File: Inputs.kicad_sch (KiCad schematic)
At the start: 2 parts, among them J14 Digital Inputs

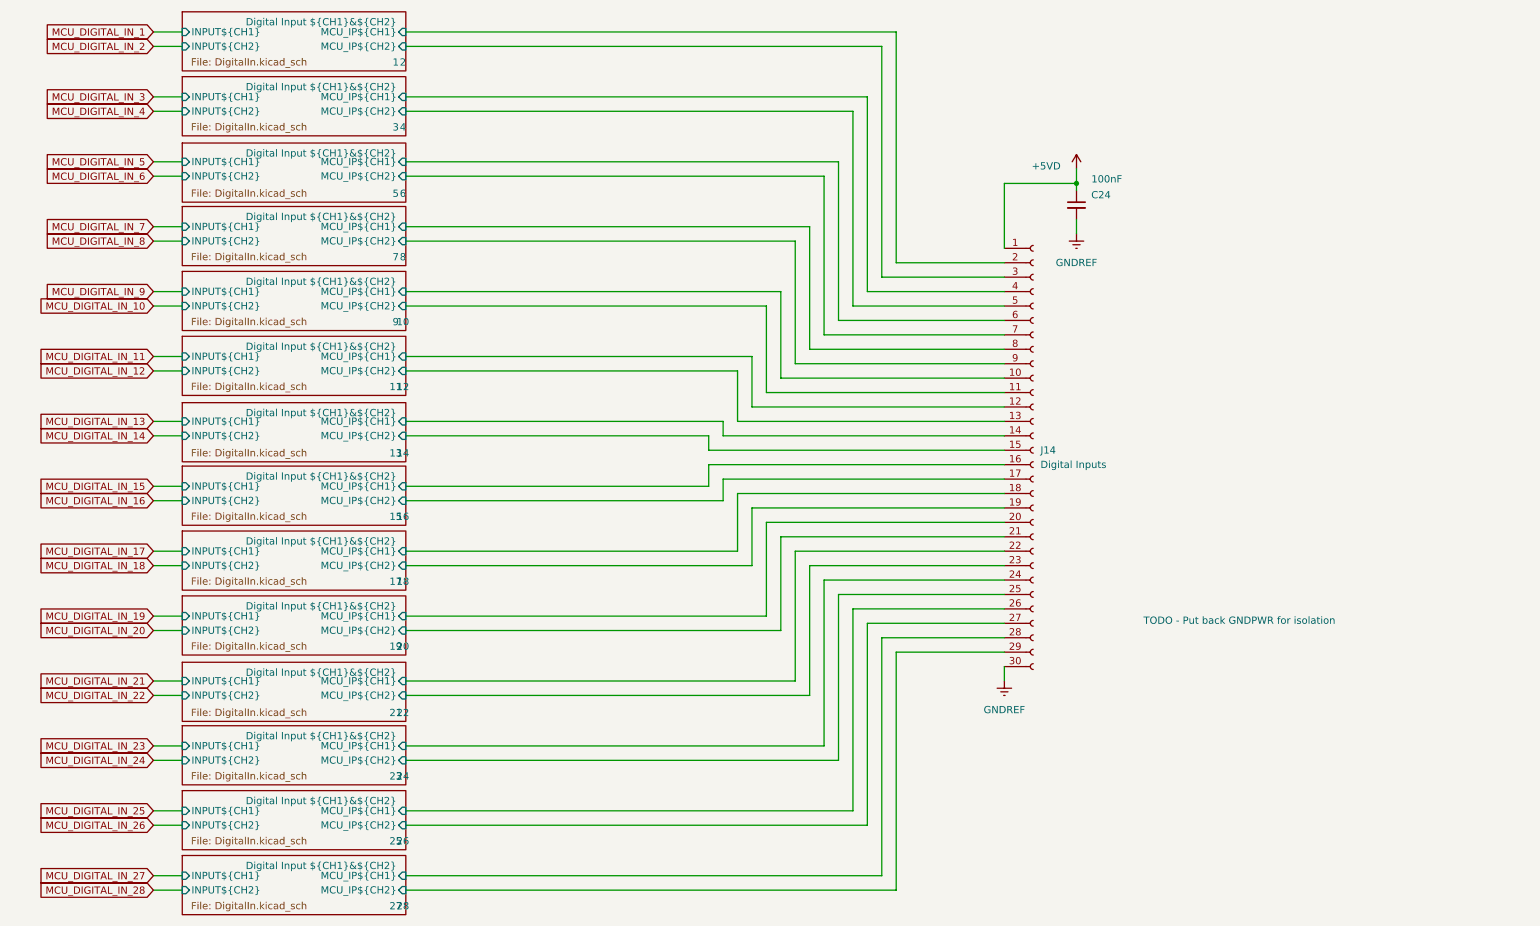
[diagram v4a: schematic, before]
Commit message: Dropped number of IO on design to make more room. Created the new footprints to suit them, updates to BOM and ran some traces on the PCB.
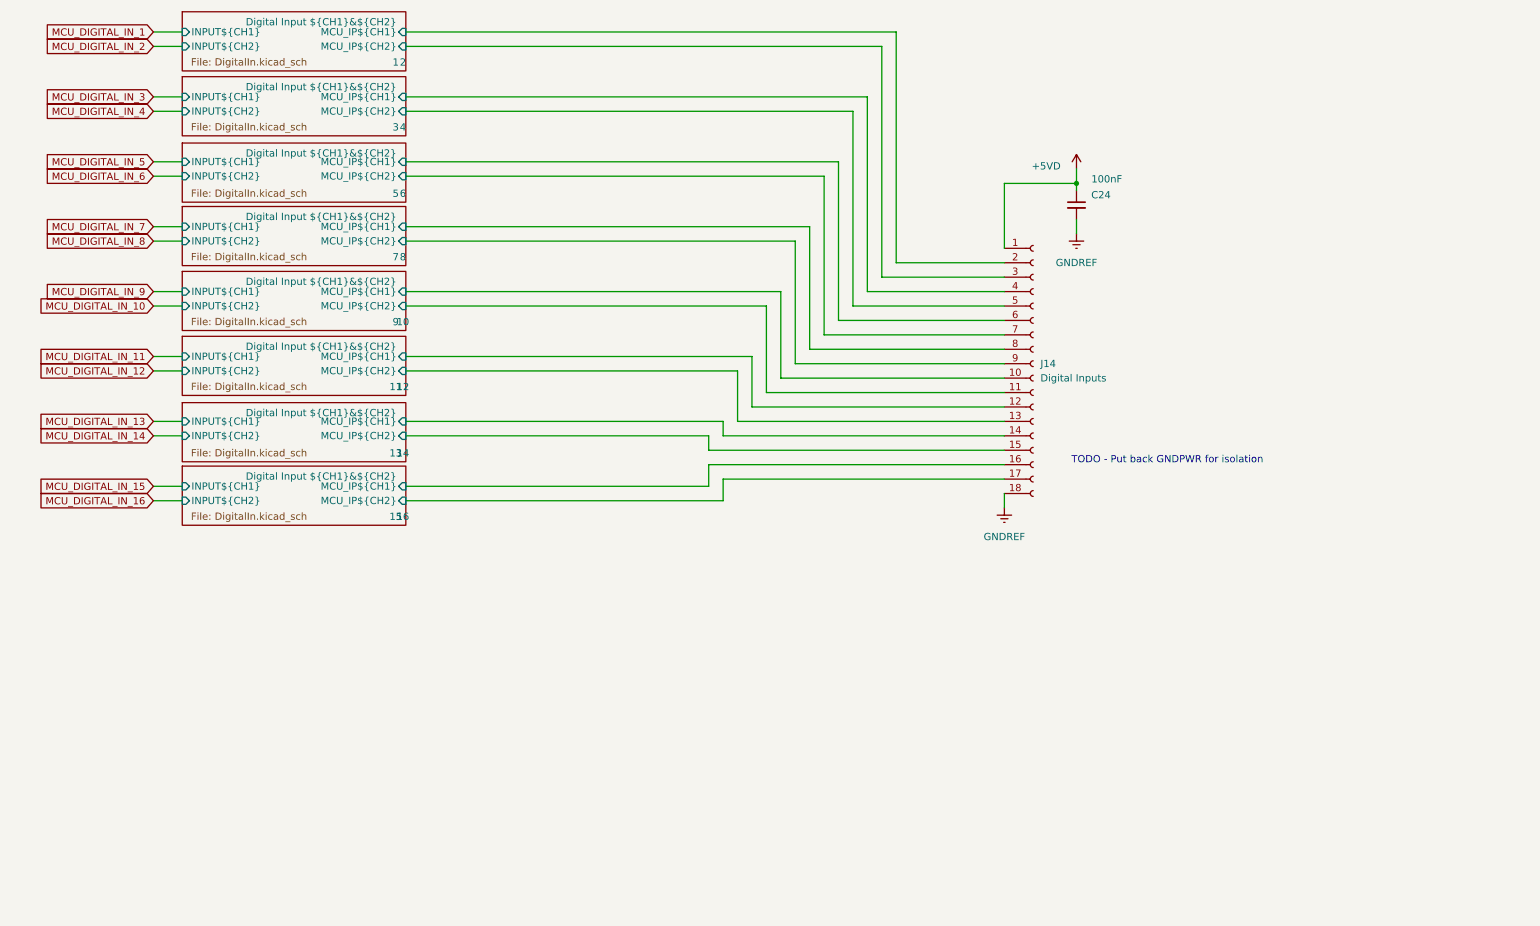
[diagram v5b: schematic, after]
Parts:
- J14: footprint EBWA_06_A:CONN_EBWA-30-A_ADM -> EBWA_06_A:CONN_EBWA-18-A_ADM; symbol Connector:Conn_01x30_Socket -> Connector:Conn_01x18_Socket
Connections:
- net Digital Input ${CH1}&${CH2}/MCU_IP${CH1} is gone; now on net GNDREF: J14.18 (Pin_18)
- net Digital Input ${CH1}&${CH2}/MCU_IP${CH1} is gone; now on net Digital Input ${CH1}&${CH2}/MCU_IP${CH1}: J14.8 (Pin_8)
- net Digital Input ${CH1}&${CH2}/MCU_IP${CH2} is gone; now on net Digital Input ${CH1}&${CH2}/MCU_IP${CH2}: J14.9 (Pin_9)
- net Digital Input ${CH1}&${CH2}/MCU_IP${CH1}: no longer J14.10 (Pin_10)
- net Digital Input ${CH1}&${CH2}/MCU_IP${CH2}: no longer J14.11 (Pin_11)
- net GNDREF: no longer J14.30 (Pin_30)
- removed net Digital Input ${CH1}&${CH2}/MCU_IP${CH1}: J14.20 (Pin_20)
- removed net Digital Input ${CH1}&${CH2}/MCU_IP${CH1}: J14.22 (Pin_22)
- removed net Digital Input ${CH1}&${CH2}/MCU_IP${CH1}: J14.24 (Pin_24)
- removed net Digital Input ${CH1}&${CH2}/MCU_IP${CH1}: J14.26 (Pin_26)
- removed net Digital Input ${CH1}&${CH2}/MCU_IP${CH1}: J14.28 (Pin_28)
- removed net Digital Input ${CH1}&${CH2}/MCU_IP${CH2}: J14.19 (Pin_19)
- removed net Digital Input ${CH1}&${CH2}/MCU_IP${CH2}: J14.21 (Pin_21)
- removed net Digital Input ${CH1}&${CH2}/MCU_IP${CH2}: J14.23 (Pin_23)
- removed net Digital Input ${CH1}&${CH2}/MCU_IP${CH2}: J14.25 (Pin_25)
- removed net Digital Input ${CH1}&${CH2}/MCU_IP${CH2}: J14.27 (Pin_27)
- removed net Digital Input ${CH1}&${CH2}/MCU_IP${CH2}: J14.29 (Pin_29)
- new net Digital Input ${CH1}&${CH2}/MCU_IP${CH1}: J14.10 (Pin_10)
- new net Digital Input ${CH1}&${CH2}/MCU_IP${CH2}: J14.11 (Pin_11)

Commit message: New optocoupler part choice, removed digikey BOM as have started inputting them into symbol fields. Re-enabled all disabled parts for now and will re-design power supplies soon.
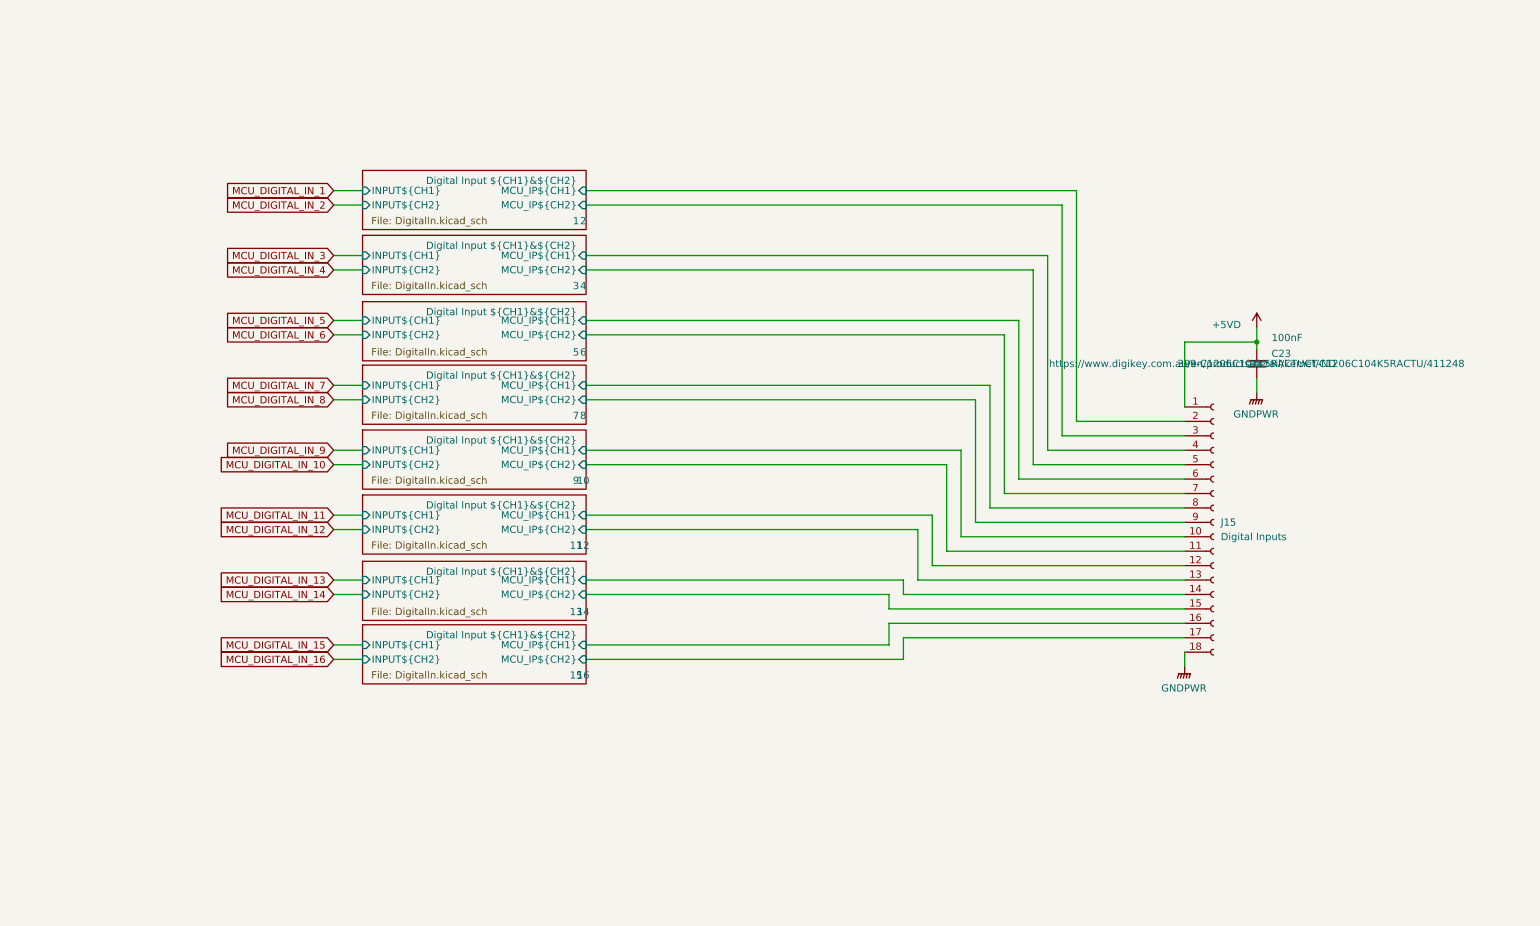
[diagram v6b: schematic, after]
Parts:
- C23: renamed from C24; Digikey Part Number (none) -> 399-C1206C104K5RACTUCT-ND; Digikey URL (none) -> https://www.digikey.com.au/en/products/detail/kemet/C1206C1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
- renumbered J14 to J15
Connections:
- net Digital Input ${CH1}&${CH2}/MCU_IP${CH1} is gone; now on net Digital Input ${CH1}&${CH2}/MCU_IP${CH1}: J15.8 (Pin_8)
- net Digital Input ${CH1}&${CH2}/MCU_IP${CH2} is gone; now on net Digital Input ${CH1}&${CH2}/MCU_IP${CH2}: J15.9 (Pin_9)
- net Digital Input ${CH1}&${CH2}/MCU_IP${CH1}: no longer J15.10 (Pin_10)
- net Digital Input ${CH1}&${CH2}/MCU_IP${CH2}: no longer J15.11 (Pin_11)
- net GNDREF renamed GNDPWR
- new net Digital Input ${CH1}&${CH2}/MCU_IP${CH1}: J15.10 (Pin_10)
- new net Digital Input ${CH1}&${CH2}/MCU_IP${CH2}: J15.11 (Pin_11)
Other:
- note removed: "TODO - Put back GNDPWR for isolation"
- moved on the sheet: C23, J15

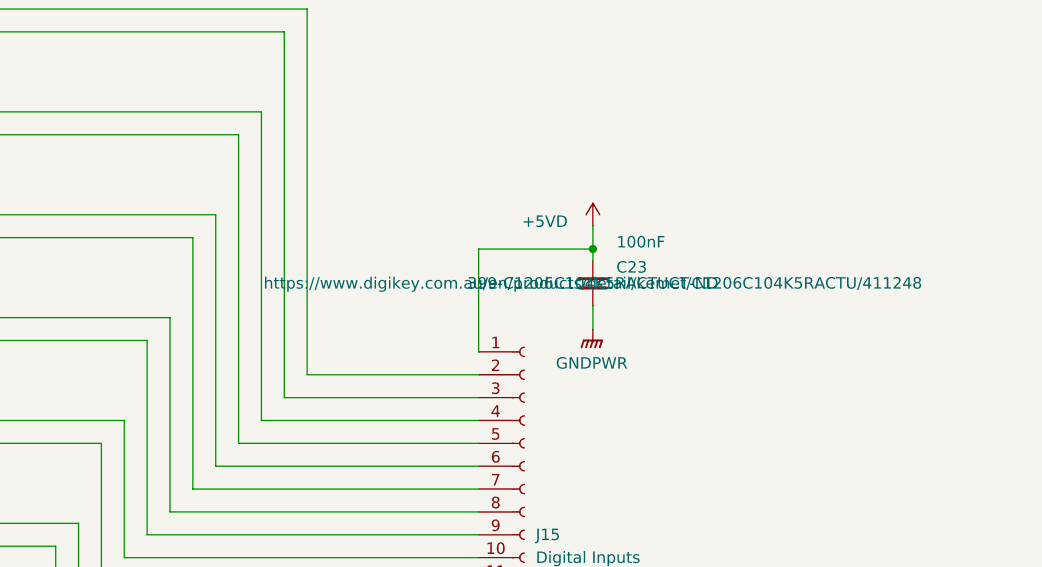
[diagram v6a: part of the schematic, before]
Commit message: fix to annoying additional symbol fields displaying when we didn't want them to.
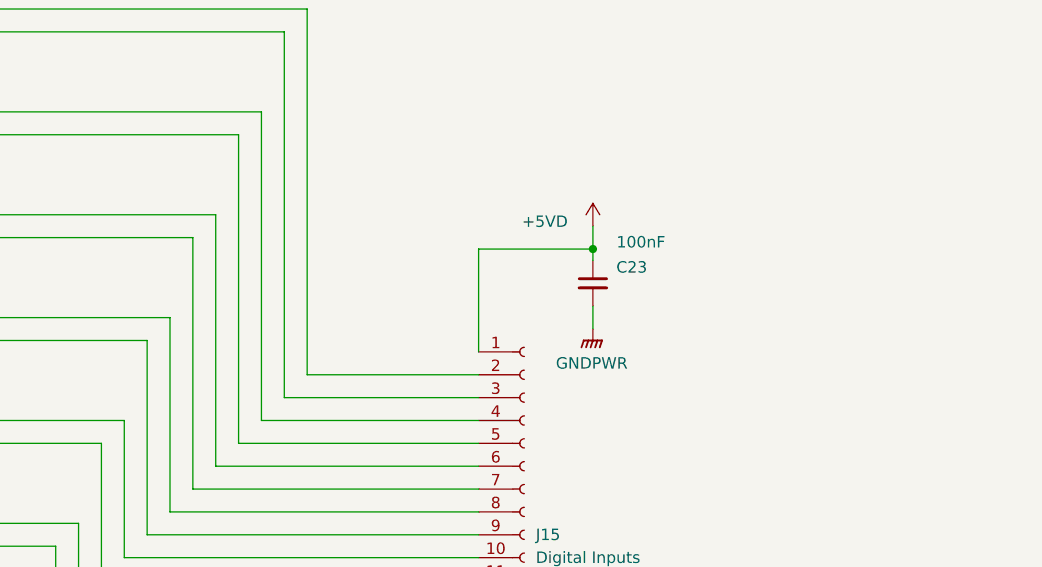
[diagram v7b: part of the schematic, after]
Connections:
- net Digital Input ${CH1}&${CH2}/MCU_IP${CH1} is gone; now on net Digital Input ${CH1}&${CH2}/MCU_IP${CH1}: J15.8 (Pin_8)
- net Digital Input ${CH1}&${CH2}/MCU_IP${CH2} is gone; now on net Digital Input ${CH1}&${CH2}/MCU_IP${CH2}: J15.9 (Pin_9)
- net Digital Input ${CH1}&${CH2}/MCU_IP${CH1}: no longer J15.10 (Pin_10)
- net Digital Input ${CH1}&${CH2}/MCU_IP${CH2}: no longer J15.11 (Pin_11)
- new net Digital Input ${CH1}&${CH2}/MCU_IP${CH1}: J15.10 (Pin_10)
- new net Digital Input ${CH1}&${CH2}/MCU_IP${CH2}: J15.11 (Pin_11)
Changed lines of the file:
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@@
 					(size 1.27 1.27)
 				)
+				(hide yes)
 			)
 		)
@@
 					(size 1.27 1.27)
 				)
+				(hide yes)
 			)
 		)
@@
 					(size 1.27 1.27)
 				)
+				(hide yes)
 			)
 		)
@@
 					(size 1.27 1.27)
 				)
+				(hide yes)
 			)
 		)

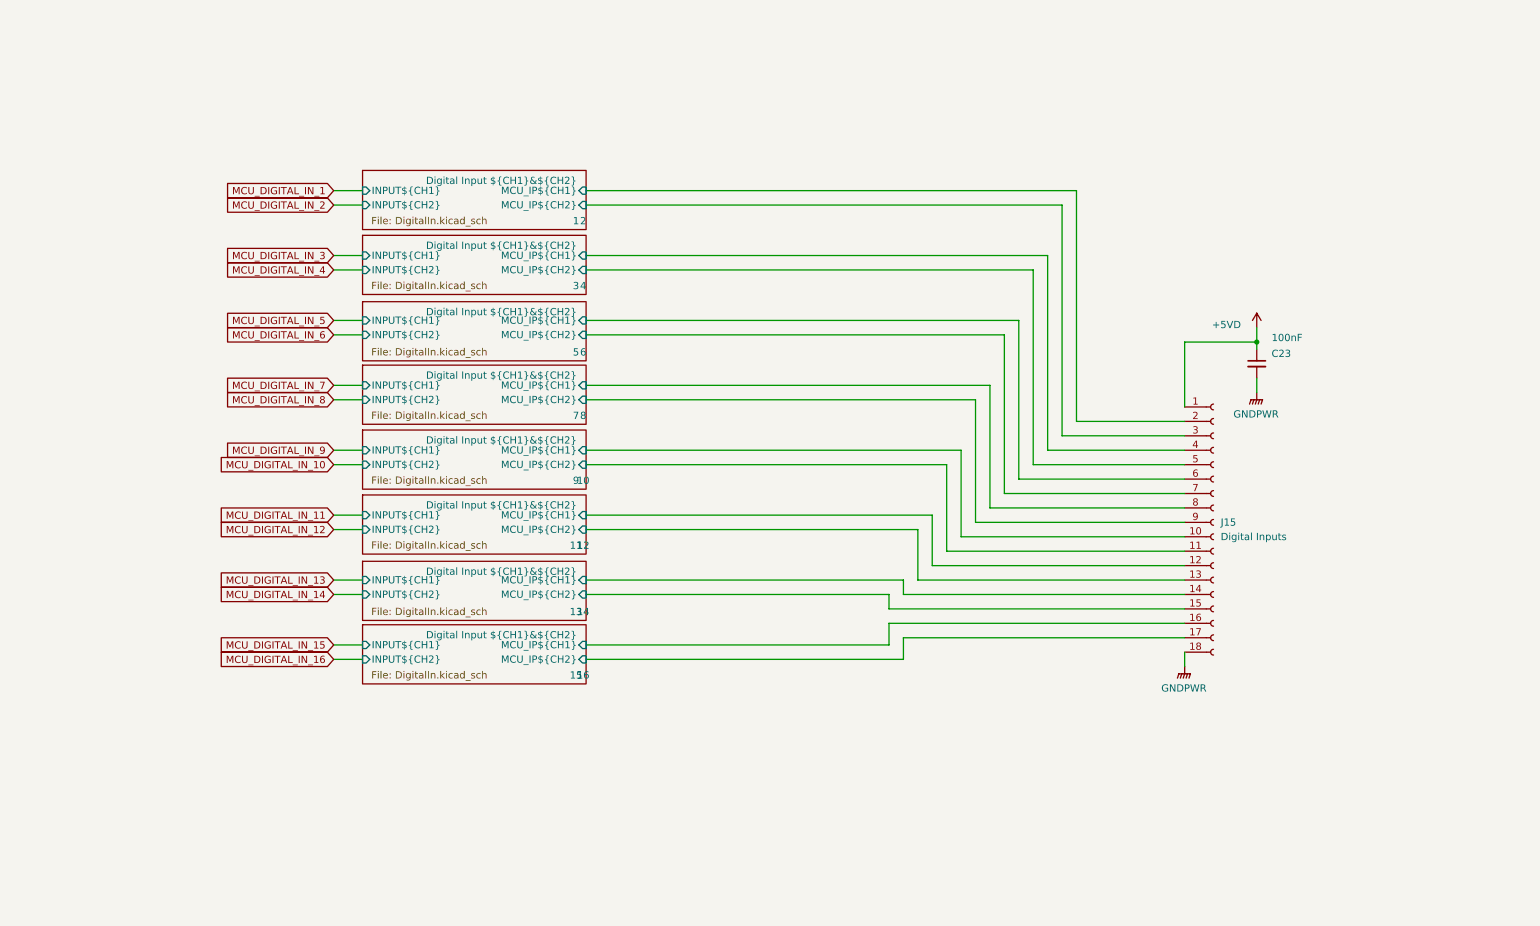
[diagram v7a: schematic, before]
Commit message: BOM consolidation for various resistors. Moved BOM into symbol libraries and updated supplimentary BOM. Switched IO optical isolation circuitry to a more cost effective part.
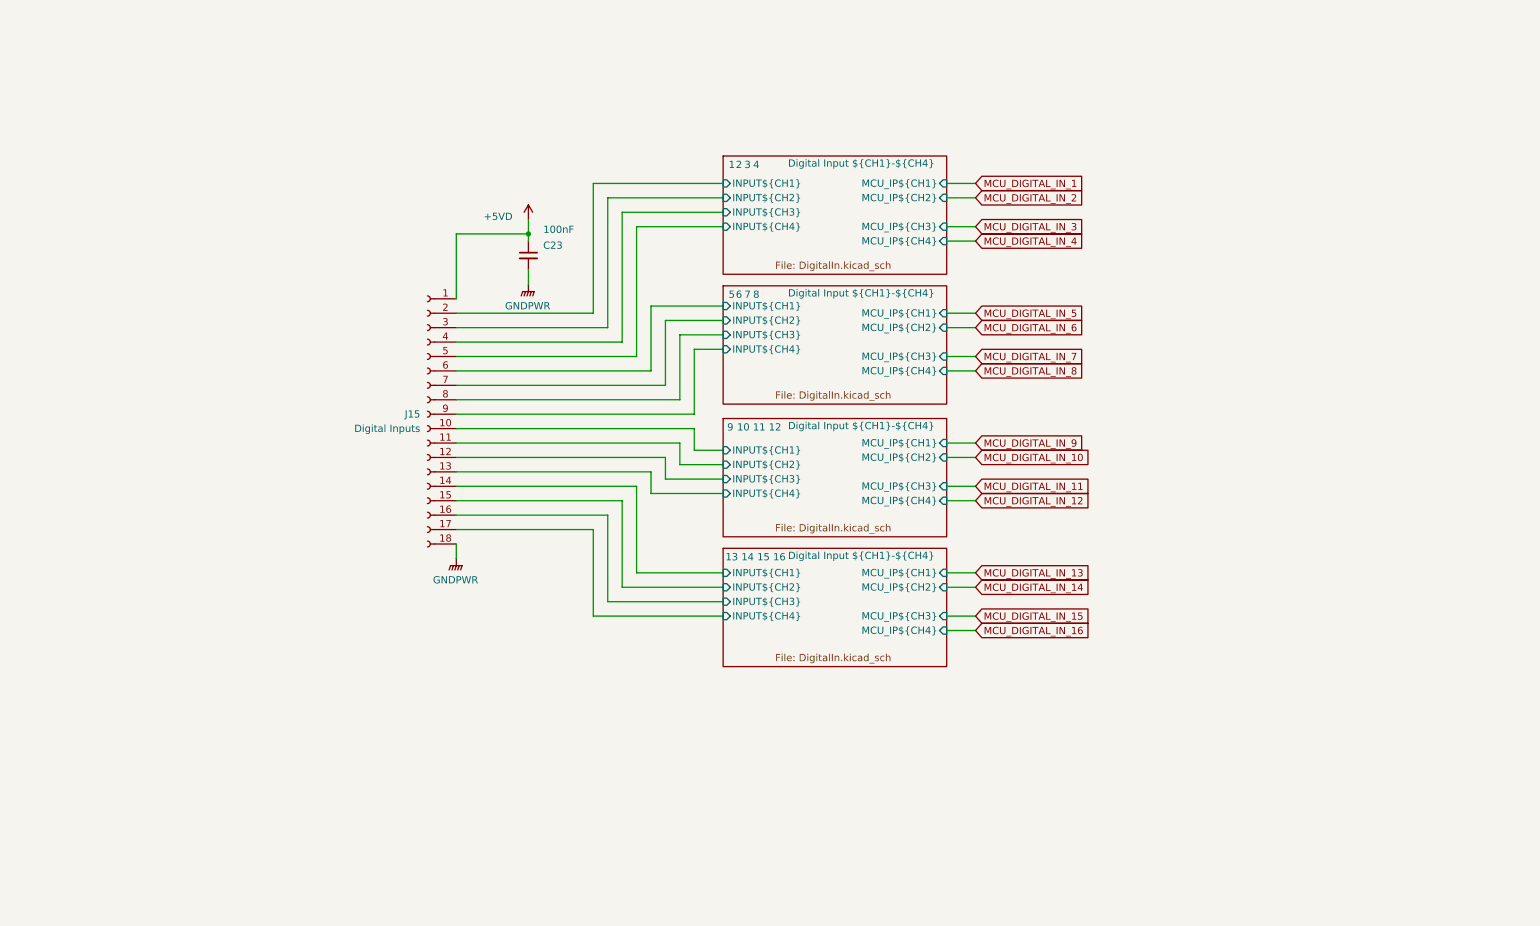
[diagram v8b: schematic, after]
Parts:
- J15: Digikey Part Number (none) -> See Manual BOM; Digikey URL (none) -> See Manual BOM
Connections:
- net Digital Input ${CH1}&${CH2}/MCU_IP${CH1} renamed Digital Input ${CH1}-${CH4}/INPUT${CH1} (x4)
- net Digital Input ${CH1}&${CH2}/MCU_IP${CH1} renamed Digital Input ${CH1}-${CH4}/INPUT${CH3} (x4)
- net Digital Input ${CH1}&${CH2}/MCU_IP${CH2} renamed Digital Input ${CH1}-${CH4}/INPUT${CH2} (x4)
- net Digital Input ${CH1}&${CH2}/MCU_IP${CH2} renamed Digital Input ${CH1}-${CH4}/INPUT${CH4} (x4)
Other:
- removed sheet Digital Input ${CH1}&${CH2}
- added sheet Digital Input ${CH1}-${CH4} (DigitalIn.kicad_sch)
- moved on the sheet: C23, J15
